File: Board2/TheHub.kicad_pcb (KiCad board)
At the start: 2 copper layers, 118.7 x 184.1 mm, 59 parts, among them J1 Actuator Fdbk Conn, J11 RFD900, J12 I2C_1 Test Point, J13 I2C_2 Test Point, J15 GPIO Test, J16 I2C_3 Test Point, J17 12V OUT, J2 QuadEnc_Conn, J23 NucleoRight, J5 NucleoLeft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

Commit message: Remove previous components from the board
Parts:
- removed J1: Actuator Fdbk Conn, Pin_Headers:Pin_Header_Straight_2x03_Pitch2.54mm
- removed J12: I2C_1 Test Point, Pin_Headers:Pin_Header_Straight_1x03_Pitch2.54mm
- removed J13: I2C_2 Test Point, Pin_Headers:Pin_Header_Straight_1x03_Pitch2.54mm
- removed J16: I2C_3 Test Point, Pin_Headers:Pin_Header_Straight_1x03_Pitch2.54mm
- removed J2: QuadEnc_Conn, Pin_Headers:Pin_Header_Straight_1x04_Pitch2.54mm
- removed J23: NucleoRight, FoxWestern:NucleoSocketStrip
- removed J5: NucleoLeft, FoxWestern:NucleoSocketStrip
- removed R10, R11, R12, R3, R4, R5: 2.2K, Resistors_SMD:R_0805
- removed U1: Datalogger, FoxWestern:Datalogger
- removed U10: ADXL377, FoxWestern:ADXL377
- removed U11: BNO055, FoxWestern:BNO055
- removed U12: MPL115A2, FoxWestern:MPL115A2
- removed U13: GPS, FoxWestern:Adafruit_GPS
- removed U2: DS3231, FoxWestern:DS3231
- removed U8: MCP9808, FoxWestern:MCP9808
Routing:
- net +3V3: track 396.3 -> 10.4 mm, vias 6 -> 0
- net /PB7: track 299.4 -> 0.00 mm, vias 5 -> 0
- net /PB6: track 256.6 -> 0.00 mm, vias 1 -> 0
- net /PC9: track 101.7 -> 0.00 mm
- net /PD2: track 92.2 -> 0.00 mm
- net /PB10: track 82.8 -> 0.00 mm, vias 1 -> 0
- net /PA11: track 81.4 -> 0.00 mm, vias 1 -> 0
- net /PB5: track 80.1 -> 0.00 mm, vias 1 -> 0
- net /PA8: track 79.3 -> 0.00 mm, vias 1 -> 0
- net /PA5: track 79.0 -> 0.00 mm, vias 1 -> 0
- net /PA12: track 74.8 -> 0.00 mm, vias 1 -> 0
- net /PB4: track 63.2 -> 0.00 mm, vias 3 -> 0
- net /PA2: track 61.2 -> 0.00 mm
- net /PB3: track 60.1 -> 0.00 mm, vias 1 -> 0
- net /PA3: track 54.9 -> 0.00 mm, vias 1 -> 0
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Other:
- board text removed: "3v3"
- board text removed: "Analog Feedback"
- board text removed: "I2C_1"
- board text removed: "I2C_2"
- board text removed: "I2C_3"
- board text removed: "Nucleo STM32F411RE"
- board text removed: "PA11 TX6"
- board text removed: "PA12 RX6"
- board text removed: "PA2 TX2"
- board text removed: "PA3 RX2"
- board text removed: "PA6"
- board text removed: "PA7"
- board text removed: "PB13"
- board text removed: "PB14"
- board text removed: "PC0"
- board text removed: "PC1"
- board text removed: "PC4"
- board text removed: "PC5"
- board text removed: "PWM"
- board text removed: "Quad Enc"
- board text removed: "SCL"
- board text removed: "SDA"

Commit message: Relayout Hub 2 Board
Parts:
- added J1: Actuator Fdbk Conn, Pin_Headers:Pin_Header_Straight_2x03_Pitch2.54mm, F.Cu at (65.6, 142.0)
- added J12: I2C_1 Test Point, Pin_Headers:Pin_Header_Straight_1x03_Pitch2.54mm, F.Cu at (67.0, 168.3)
- added R10: 0, Resistors_SMD:R_0805, F.Cu at (87.9, 162.2)
- added R3: 2.2K, Resistors_SMD:R_0805, F.Cu at (97.0, 164.7)
- added R4: 2.2K, Resistors_SMD:R_0805, F.Cu at (97.0, 162.2)
- added R5: 0, Resistors_SMD:R_0805, F.Cu at (87.9, 159.6)
- added U1: FeatherM0, FoxWestern:FeatherM0, F.Cu at (81.4, 126.6)
- added U10: ADXL377, FoxWestern:ADXL377, F.Cu at (110.4, 95.4)
- added U11: BNO055, FoxWestern:BNO055, F.Cu at (128.7, 145.3)
- added U12: MPL115A2, FoxWestern:MPL115A2, F.Cu at (131.1, 156.8)
- added U2: DS3231, FoxWestern:DS3231, F.Cu at (125.0, 174.2)
- added U3: ArduinoNano, FoxWestern:ArduinoNano, F.Cu at (150.4, 131.7)
- added U4: GT-U7_GPS, FoxWestern:GT-U7_GPS, F.Cu at (154.4, 152.7)
- R6, R7, R8, R9: value 220 -> 1k
- moved ? 97.9 mm to (121.7, 104.4)
- moved D6 96.4 mm to (84.3, 98.2), turned to 0 degrees
- moved D5 93.3 mm to (84.3, 102.0), turned to 0 degrees
- moved G*** 92.2 mm to (212.6, 124.3)
- moved D4 90.7 mm to (84.3, 105.8), turned to 0 degrees
- moved D3 88.8 mm to (84.3, 109.7), turned to 0 degrees
- moved R9 87.4 mm to (89.4, 98.2), turned to 180 degrees
- moved R8 84.0 mm to (89.4, 102.0), turned to 180 degrees
- moved R7 81.1 mm to (89.4, 105.8), turned to 180 degrees
- moved R6 78.9 mm to (89.4, 109.7), turned to 180 degrees
- moved J15 67.4 mm to (95.7, 108.4), turned to 180 degrees
- moved ? 67.3 mm to (121.7, 134.6)
- moved ? 55.2 mm to (139.6, 175.9)
- moved ? 55.2 mm to (100.3, 175.9)
- moved ? 55.2 mm to (66.0, 175.9)
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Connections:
- net /PA6 renamed /Status3
- net /PA7 renamed /Status4
- net /PC4 renamed /Status1
- net /PC5 renamed /Status2
- J11 pad 7: /PA11 -> /RFD900_RX
- J11 pad 9: /PA12 -> /RFD900_TX
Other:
- board size 118.7 x 184.1 mm -> 118.7 x 129.5 mm
- board text added: "ADXL337 High-G Accel Analog"
- board text added: "BNO055 IMU 0x28"
- board text added: "FDBK 3.3V GND"
- board text added: "GND SCL SDA"
- board text added: "GPS GT-U7"
- board text added: "MPL115A2 Baro 0x60"
- board text added: "Status 4 (D11) Status 3 (D10) Status 2 (D9) Status 1 (D5)"
- board text added: "The Hub, Feather M0, Rev. 2 Danny Mallek 4/18/2018"
- board text removed: "0x18"
- board text removed: "0x28"
- board text removed: "0x60"
- board text removed: "0x68"
- board text removed: "Center Line"
- board text removed: "MPL115A2"
- board text removed: "The Hub, Rev. 1 Danny Mallek 1/8/2018"

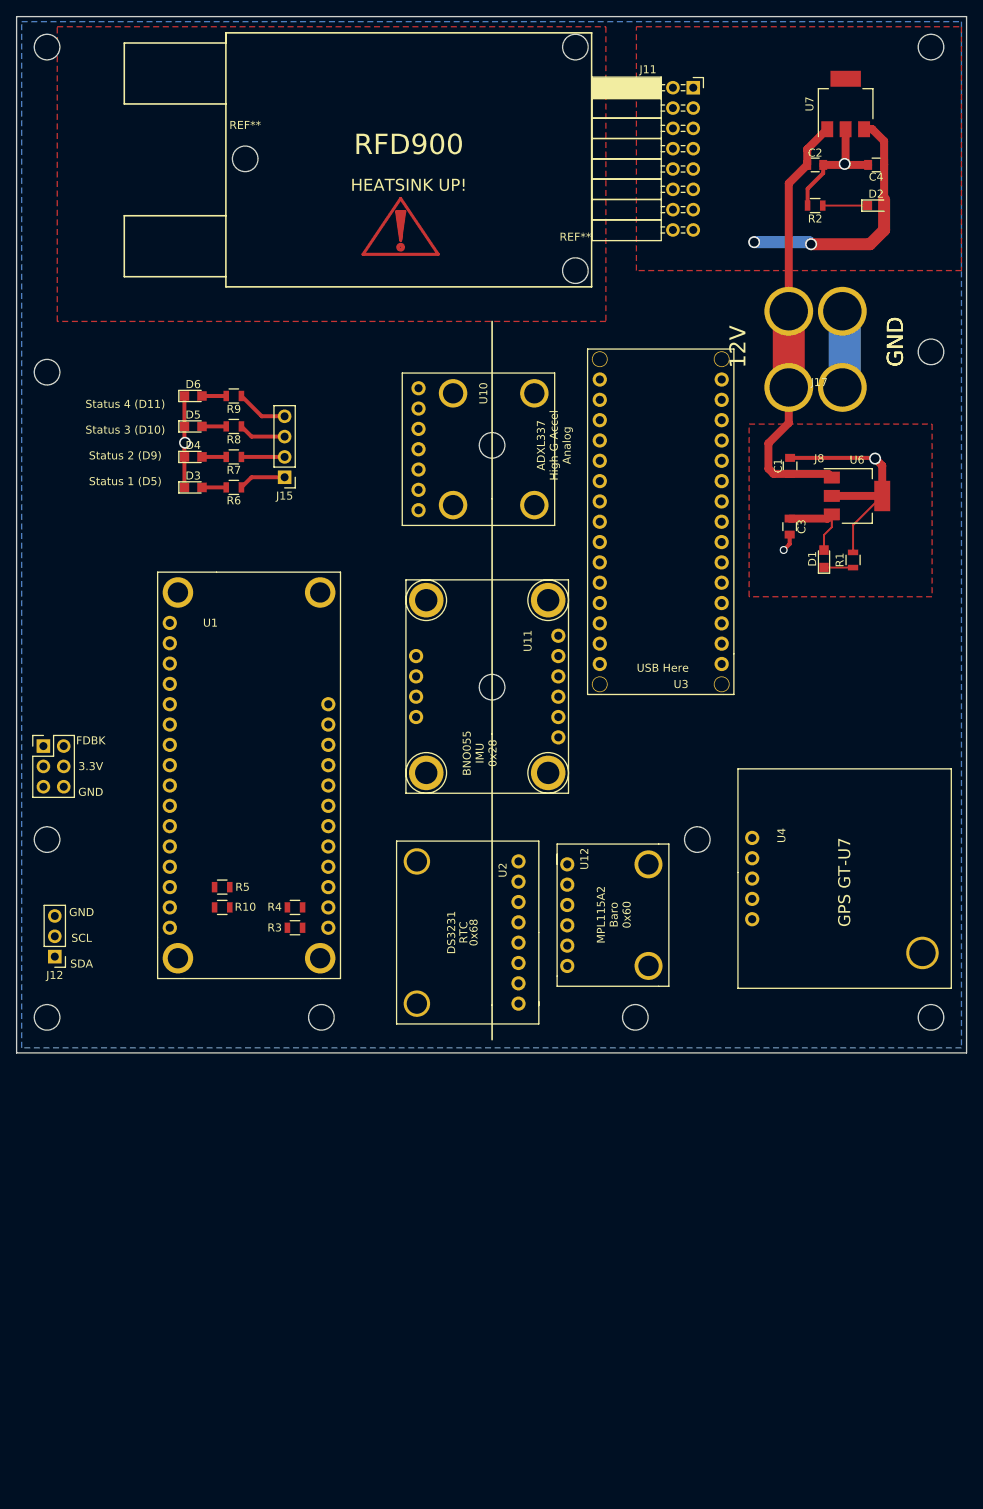
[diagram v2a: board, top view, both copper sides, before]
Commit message: Add nice text markings
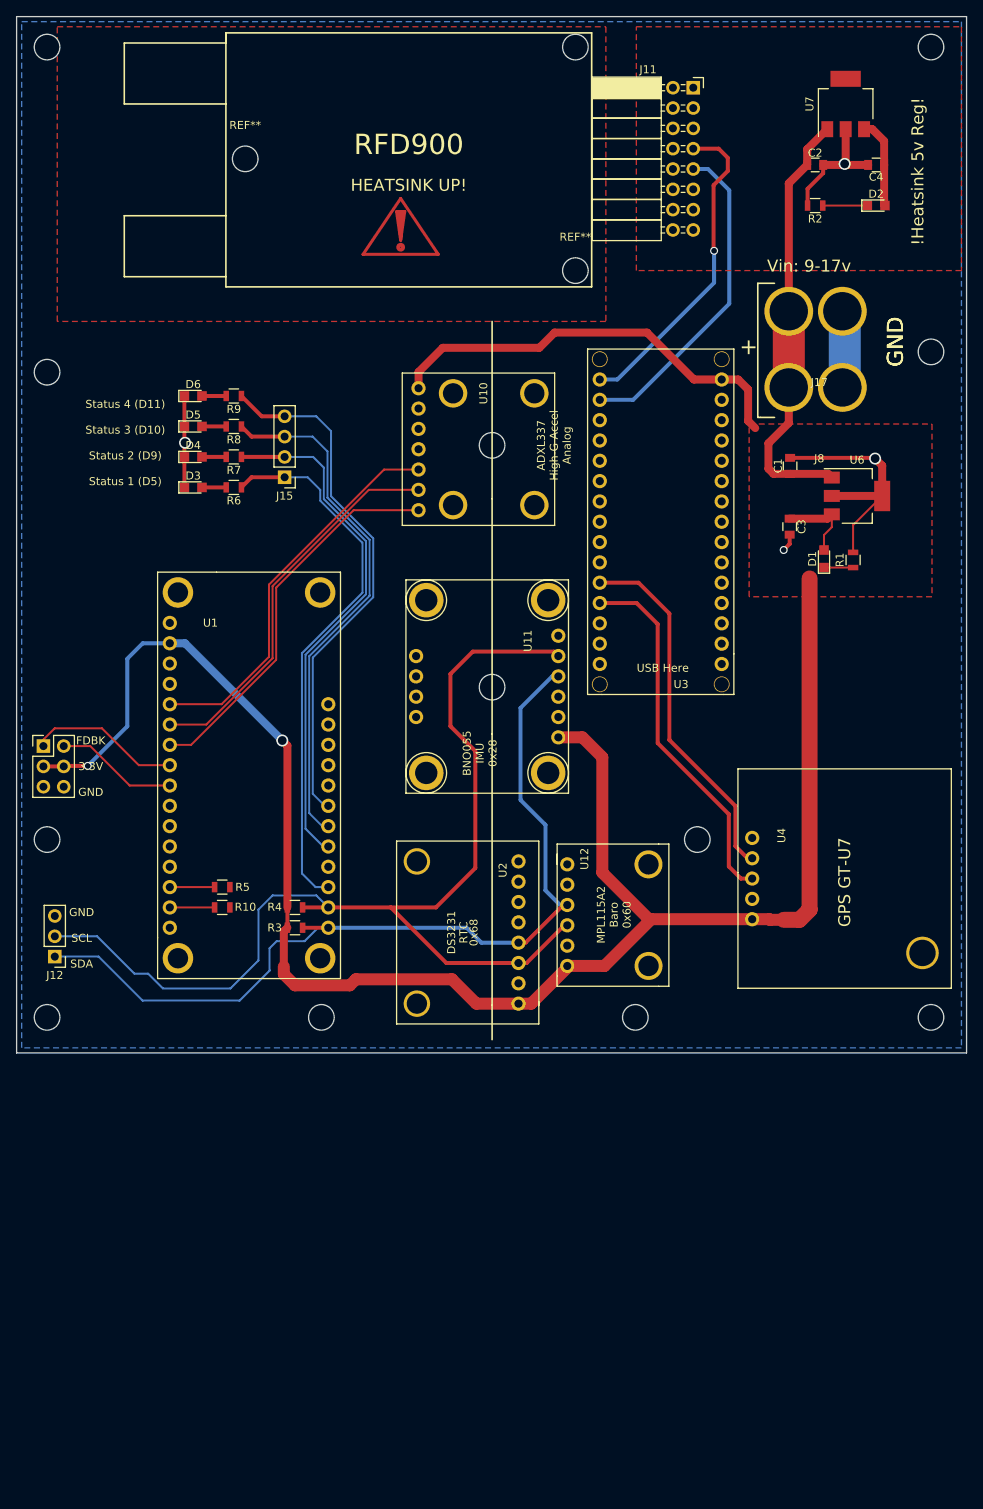
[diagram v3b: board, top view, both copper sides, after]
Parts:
- moved G*** 49.9 mm to (164.6, 138.0)
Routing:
- net +3V3: track 10.4 -> 304.3 mm, vias 0 -> 2
- net /SCL_1: track 0.00 -> 137.0 mm
- net /SDA_1: track 0.00 -> 111.6 mm
- net /Status1: track 5.93 -> 68.3 mm
- net /Status4: track 6.45 -> 66.2 mm
- net /Status3: track 5.93 -> 65.6 mm
- net /Status2: track 5.40 -> 65.1 mm
- net /A1: track 0.00 -> 48.5 mm
- net /A0: track 0.00 -> 48.5 mm
- net /A2: track 0.00 -> 48.5 mm
- net /GPS_RX: track 0.00 -> 45.9 mm
- net /GPS_TX: track 0.00 -> 45.5 mm
- net /RFD900_TX: track 0.00 -> 40.9 mm
- net /RFD900_RX: track 0.00 -> 40.5 mm, vias 0 -> 1
- net +5V: track 32.1 -> 11.2 mm, vias 2 -> 0
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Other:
- board text added: "!Heatsink 5v Reg!"
- board text added: "+"
- board text added: "Vin: 9-17v"
- board text removed: "12V"

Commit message: Modify RFD footprint, generate Gerbs
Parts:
- removed R10, R5: 0, Resistors_SMD:R_0805
- moved REF** 3.43 mm to (94.2, 68.6)
- moved REF** 1.45 mm to (131.5, 81.2)
- moved ? 1.34 mm to (131.5, 55.8)
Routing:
- net Net-(R5-Pad1): track 5.60 -> 0.00 mm
- net Net-(R10-Pad1): track 5.60 -> 0.00 mm

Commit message: Add most of the schematic fo the new board
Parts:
- removed D6: LED, LEDs:LED_0805
- removed R9: 1k, Resistors_SMD:R_0805
- added J2: Conn_01x03, Pin_Headers:Pin_Header_Straight_1x03_Pitch2.54mm, F.Cu at (65.5, 130.7)
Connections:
- J15 pad 4: /Status4 -> GND
- U1 pad 23: /Status4 -> /ActuatorPWM
- U1 pad 24: Net-(U1-Pad24) -> /ActuatorDir
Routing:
- net /ActuatorPWM: track 0.00 -> 80.7 mm, vias 0 -> 1
- net /ActuatorDir: track 0.00 -> 71.6 mm, vias 0 -> 2
- net /Status4: track 66.2 -> 0.00 mm
- net Net-(D6-Pad2): track 3.03 -> 0.00 mm
- net GND: track 70.1 -> 68.6 mm
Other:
- board text added: "Status 3 (D10) Status 2 (D9) Status 1 (D5)"
- board text removed: "Status 4 (D11) Status 3 (D10) Status 2 (D9) Status 1 (D5)"
